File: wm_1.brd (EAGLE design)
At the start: 160 x 100 mm, 26 parts, among them IC2 DS1813-SMD, IC4 MEGA8-AI, T1 MMBT3904, T2 BT138-V, X1 MKDSN1,5/2-5,08, X2 MKDSN1,5/2-5,08

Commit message: wip
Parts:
- added R8, R9: 1k, rcl:R1206
- added SJ1: (no value), MyLib:SOLDERJUMPER_REFLOW
- moved C3 75.3 mm to (72.1, 7.68), turned to 180 degrees
- moved C16 70.3 mm to (35.3, -21.8), turned to 270 degrees
- moved C18 66.4 mm to (35.6, 3.81)
- moved C17 66.2 mm to (45.5, 3.94)
- moved Q1 66.1 mm to (40.2, -3.30)
- moved R5 65.1 mm to (78.4, 7.68)
- moved R7 63.6 mm to (72.1, 15.9), turned to 180 degrees
- moved IC4 62.2 mm to (36.0, -13.1)
- moved JP1 57.9 mm to (22.2, -15.4)
- moved R6 57.6 mm to (78.4, 15.9), turned to 180 degrees
- moved C4 56.8 mm to (72.1, 11.9), turned to 180 degrees
- moved IC2 56.3 mm to (21.0, -5.52)
- moved OK2 38.1 mm to (61.5, 11.7)
- moved C1 35.2 mm to (36.7, 49.1)
- moved C2 35.2 mm to (68.5, 49.1)
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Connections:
- new net N$17: OK2.1, R8.1
- new net N$18: OK1.5, R9.2, SJ1.1
- net +5V: now also R9.1
- net 485_R/W: now also R8.2; no longer OK2.1
- net GND: now also OK1.4
- net GROUND: now also R1.1, X1.2; no longer R2.1, X1.1
- net HOT: now also R2.1, X1.1; no longer R1.1, X1.2
- net INT0: now also SJ1.2

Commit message: wip
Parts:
- removed X1, X2: MKDSN1,5/2-5,08, con-phoenix-508:MKDSN1,5/2-5,08
- added HLK1: HLK-PM013W, hi-link:HLK-PM01
- added IN, OUT: MKDSN1,5/2-5,08, con-phoenix-508:MKDSN1,5/2-5,08
- added U$1: 2X16LCDSIDE, MyDisplays:2X16LCDSIDE
- moved OK1 56.0 mm to (73.6, 35.0), turned to 180 degrees
- moved C16 54.1 mm to (26.8, 31.6), turned to 90 degrees
- moved R4 54.0 mm to (81.5, 41.4)
- moved R8 53.8 mm to (19.7, 11.4), turned to 90 degrees
- moved R9 42.3 mm to (15.7, 11.4)
- moved SJ1 39.5 mm to (16.5, 15.8), turned to 0 degrees
- moved JP1 38.8 mm to (42.5, 17.7), flipped to the bottom, turned to 270 degrees
- moved IC4 36.1 mm to (26.5, 21.7), turned to 90 degrees
- moved IC2 27.6 mm to (43.5, 10.5), turned to 180 degrees
- moved C17 20.0 mm to (25.7, 6.41), turned to 180 degrees
- moved Q1 18.0 mm to (29.7, 11.3), turned to 180 degrees
- moved C1 15.0 mm to (51.4, 52.5)
- moved T2 14.5 mm to (97.9, 13.4), flipped to the bottom, turned to 180 degrees
- moved B1 11.5 mm to (71.9, 50.7)
- moved D1 11.5 mm to (61.5, 50.9)
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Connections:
- net 485_R/W renamed ON/OFF
- removed net N$10: IC4.23
- removed net N$11: IC4.24
- removed net N$12: IC4.25
- removed net N$13: IC4.26
- removed net SPI0: IC4.19
- new net D4: IC4.23, U$1.11
- new net D5: IC4.24, U$1.12
- new net D6: IC4.25, U$1.13
- new net D7: IC4.26, U$1.14
- new net E: IC4.22, U$1.6
- new net RS: IC4.19, U$1.4
- net +5V: now also HLK1.P$4
- net GND: now also HLK1.P$3
- net GROUND: now also HLK1.P$2, IN.2, OUT.1, R2.1; no longer R1.1, X1.2, X2.2
- net HOT: now also HLK1.P$1, IN.1, R1.1; no longer R2.1, X1.1
- net INT0: no longer SJ1.2
- net INT1: now also SJ1.2
- net LOAD: now also OUT.2; no longer X2.1
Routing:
- net HOT: track 0.00 -> 66.2 mm, vias 0 -> 1
- net LOAD: track 0.00 -> 46.2 mm
- net RESET: track 0.00 -> 45.4 mm, vias 0 -> 2
- net GROUND: track 0.00 -> 33.2 mm
- net SCK: track 0.00 -> 27.0 mm
- net N$5: track 24.6 -> 50.0 mm
- net +5V: track 0.00 -> 22.4 mm
- net GND: track 0.00 -> 21.9 mm
- net N$7: track 0.00 -> 17.6 mm
- net MISO: track 0.00 -> 17.2 mm
- net MOSI: track 0.00 -> 16.4 mm
- net N$14: track 0.00 -> 14.1 mm
- net N$26: track 0.00 -> 12.5 mm
- net N$8: track 0.00 -> 7.45 mm
- net N$16: track 0.00 -> 6.13 mm
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
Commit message: wip
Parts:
- moved R9 48.5 mm to (62.0, 26.0), turned to 180 degrees
- moved SJ1 39.8 mm to (54.9, 26.4), turned to 180 degrees
- moved R8 39.0 mm to (58.5, 15.0), turned to 180 degrees
- moved C18 30.2 mm to (9.59, -11.9)
- moved C17 30.2 mm to (1.71, -11.9)
- moved Q1 30.2 mm to (5.65, -6.99)
- moved IC4 13.5 mm to (27.0, 35.1)
- moved OK1 13.0 mm to (60.6, 35.3)
- moved C16 12.6 mm to (26.4, 44.2), turned to 180 degrees
- moved R4 11.8 mm to (69.8, 39.9), turned to 0 degrees
- moved C3 7.69 mm to (78.1, 8.45)
- moved C4 7.69 mm to (78.1, 12.6)
- moved R7 7.69 mm to (78.1, 16.6)
- moved HLK1 7.69 mm to (74.3, 12.4)
- moved OK2 7.69 mm to (67.6, 12.4)
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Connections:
- net N$14: no longer IC4.8
- net N$26: no longer IC4.7
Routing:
- net GND: track 21.9 -> 158.1 mm
- net +5V: track 22.4 -> 77.1 mm
- net RS: track 0.00 -> 27.0 mm
- net E: track 0.00 -> 19.7 mm
- net D7: track 0.00 -> 17.6 mm
- net D5: track 0.00 -> 16.6 mm
- net D4: track 0.00 -> 16.0 mm
- net RESET: track 45.4 -> 60.5 mm
- net MISO: track 17.2 -> 32.0 mm
- net MOSI: track 16.4 -> 31.2 mm
- net SCK: track 27.0 -> 41.7 mm
- net N$7: track 17.6 -> 3.46 mm
- net D6: track 0.00 -> 12.0 mm
- net N$18: track 0.00 -> 9.91 mm
- net N$5: track 50.0 -> 43.9 mm
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
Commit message: wip
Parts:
- removed C16: 0.1, rcl:C0805
- removed C17, C18: (no value), rcl:C0805
- removed IC4: MEGA8-AI, atmel:TQFP32-08
- removed Q1: (no value), crystal:SM49
- removed SJ1: (no value), MyLib:SOLDERJUMPER_REFLOW
- removed U$1: 2X16LCDSIDE, MyDisplays:2X16LCDSIDE
- added IC1: TINY13-20MM0, atmel:10M1
- moved IN 87.1 mm to (16.6, 66.7), turned to 90 degrees
- moved T2 76.2 mm to (50.0, 68.3), turned to 0 degrees
- moved R1 74.3 mm to (12.3, 46.0), turned to 0 degrees
- moved R2 74.0 mm to (12.3, 51.1), turned to 0 degrees
- moved C2 61.2 mm to (18.7, 48.6), turned to 90 degrees
- moved IC2 57.4 mm to (96.3, 32.1)
- moved R8 53.7 mm to (101.1, 47.7), turned to 0 degrees
- moved JP1 49.1 mm to (87.2, 36.9), turned to 0 degrees
- moved HLK1 48.9 mm to (27.7, 27.2), turned to 180 degrees
- moved R5 46.7 mm to (75.2, 54.2), turned to 180 degrees
- moved C3 45.9 mm to (81.5, 54.2), turned to 0 degrees
- moved B1 45.3 mm to (26.7, 48.5), turned to 90 degrees
- moved OK2 45.0 mm to (92.1, 50.2), turned to 90 degrees
- moved C4 37.6 mm to (81.5, 50.0), turned to 0 degrees
- moved OUT 34.9 mm to (107.8, 66.9)
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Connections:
- removed net D4: IC4.23, U$1.11
- removed net D5: IC4.24, U$1.12
- removed net D6: IC4.25, U$1.13
- removed net D7: IC4.26, U$1.14
- removed net E: IC4.22, U$1.6
- removed net E_RESET: IC4.13
- removed net E_SELECT: IC4.14
- removed net INT0: IC4.32
- removed net INT1: IC4.1, SJ1.2
- removed net N$14: C18.1, Q1.1
- removed net N$18: OK1.5, R9.2, SJ1.1
- removed net N$26: C17.2, Q1.2
- removed net N$61: C16.1, IC4.20
- removed net N$64: IC4.10
- removed net N$66: IC4.9
- removed net RS: IC4.19, U$1.4
- removed net RXD: IC4.30
- removed net SCL: IC4.28
- removed net SDA: IC4.27
- removed net SD_DETECT: IC4.11
- removed net SD_SELECT: IC4.12
- removed net TXD: IC4.31
- new net ZERO: OK1.5, R9.2
- net +5V: now also IC1.10; no longer IC4.18, IC4.4, IC4.6
- net GND: now also IC1.11, IC1.5; no longer C16.2, C17.1, C18.2, IC4.21, IC4.3, IC4.5
- net MISO: now also IC1.7; no longer IC4.16
- net MOSI: now also IC1.6; no longer IC4.15
- net ON/OFF: now also IC1.4; no longer IC4.2
- net RESET: now also IC1.1; no longer IC4.29
- net SCK: now also IC1.9; no longer IC4.17
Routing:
- net GND: track 158.1 -> 6.12 mm
- net +5V: track 77.1 -> 2.80 mm
- net HOT: track 71.1 -> 8.28 mm, vias 1 -> 0
- net LOAD: track 46.2 -> 6.54 mm
- net GROUND: track 38.2 -> 0.11 mm
- net SCK: track 41.7 -> 10.8 mm
- net RESET: track 60.5 -> 31.0 mm, vias 2 -> 0
- net RS: track 27.0 -> 0.00 mm
- net MISO: track 32.0 -> 6.37 mm
- net N$7: track 3.46 -> 25.1 mm
- net MOSI: track 31.2 -> 9.68 mm
- net E: track 19.7 -> 0.00 mm
- net D7: track 17.6 -> 0.00 mm
- net D5: track 16.6 -> 0.00 mm
- net D4: track 16.0 -> 0.00 mm
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
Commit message: wip
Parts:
- removed HLK1: HLK-PM013W, hi-link:HLK-PM01
- removed IC1: TINY13-20MM0, atmel:10M1
- removed IC2: DS1813-SMD, MyLib:SOT-23
- removed R9: 1k, rcl:R1206
- added F1: (no value), fuse:GSH15
- JP1: device pinhead:2X03 -> pinhead:1X03
- moved IN 54.0 mm to (4.06, 14.2), turned to 270 degrees
- moved OUT 52.9 mm to (109.1, 14.0), turned to 90 degrees
- moved OK1 36.6 mm to (62.2, 14.2)
- moved R4 36.3 mm to (59.3, 6.67)
- moved T2 35.9 mm to (54.8, 32.7)
- moved OK2 35.7 mm to (91.2, 14.5)
- moved B1 34.2 mm to (26.3, 14.3)
- moved C1 34.2 mm to (48.2, 12.8)
- moved C2 34.2 mm to (18.3, 14.4)
- moved D1 34.2 mm to (36.7, 14.1)
- moved R1 34.2 mm to (11.9, 11.8)
- moved R2 34.2 mm to (11.9, 16.9)
- moved R3 34.2 mm to (36.4, 10.2)
- moved T1 34.2 mm to (37.6, 20.5)
- moved C3 34.1 mm to (80.7, 20.1)
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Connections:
- net N$9 renamed GATE
- removed net +5V: HLK1.P$4, IC1.10, IC2.2, JP1.2, R9.1
- removed net MISO: IC1.7, JP1.1
- removed net MOSI: IC1.6, JP1.4
- removed net RESET: IC1.1, IC2.1, JP1.5
- removed net SCK: IC1.9, JP1.3
- new net N$9: F1.2, IN.1
- net GND: now also JP1.1; no longer HLK1.P$3, IC1.11, IC1.5, IC2.3, JP1.6
- net GROUND: now also R1.1; no longer HLK1.P$2, R2.1
- net HOT: now also F1.1, R2.1; no longer HLK1.P$1, IN.1, R1.1
- net ON/OFF: now also JP1.2; no longer IC1.4
- net ZERO: now also JP1.3; no longer R9.2
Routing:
- net GROUND: track 0.11 -> 130.4 mm
- net GATE: track 0.00 -> 81.9 mm, vias 0 -> 2
- net LOAD: track 6.54 -> 74.3 mm
- net ZERO: track 0.00 -> 65.4 mm
- net GND: track 6.12 -> 52.8 mm
- net RESET: track 31.0 -> 0.00 mm
- net HOT: track 8.28 -> 33.8 mm
- net SCK: track 10.8 -> 0.00 mm
- net MOSI: track 9.68 -> 0.00 mm
- net MISO: track 6.37 -> 0.00 mm
- net N$17: track 0.28 -> 6.22 mm
- net ON/OFF: track 0.00 -> 4.23 mm
- net +5V: track 2.80 -> 0.00 mm
- net N$6: track 15.4 -> 13.2 mm
- net N$16: track 6.12 -> 4.41 mm
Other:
- board size 160 x 100 mm -> 114 x 34.2 mm

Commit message: First pcb revision
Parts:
- moved T2 22.0 mm to (76.8, 31.5)
- moved F1 2.78 mm to (22.4, 27.2), flipped to the bottom, turned to 0 degrees
- moved T1 2.54 mm to (37.6, 18.0)
- moved R4 1.97 mm to (59.4, 8.64)
- moved D1 1.65 mm to (36.6, 12.4)
- moved OK1 1.52 mm to (62.2, 15.7)
- moved R3 1.48 mm to (36.2, 8.76)
- moved IN 0.19 mm to (4.06, 14.0)
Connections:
- net HOT: no longer R2.1
- net N$9: now also R2.1
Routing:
- net GATE: track 81.9 -> 149.2 mm, vias 2 -> 0
- net HOT: track 33.8 -> 63.8 mm
- net LOAD: track 74.3 -> 49.0 mm
- net N$9: track 0.00 -> 25.1 mm
- net GROUND: track 130.4 -> 122.9 mm
- net GND: track 52.8 -> 54.3 mm
- net N$4: track 15.4 -> 14.0 mm
- net N$3: track 15.2 -> 14.2 mm
- net ZERO: track 65.4 -> 64.5 mm
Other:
- board size 114 x 34.2 mm -> 114.1 x 34 mm

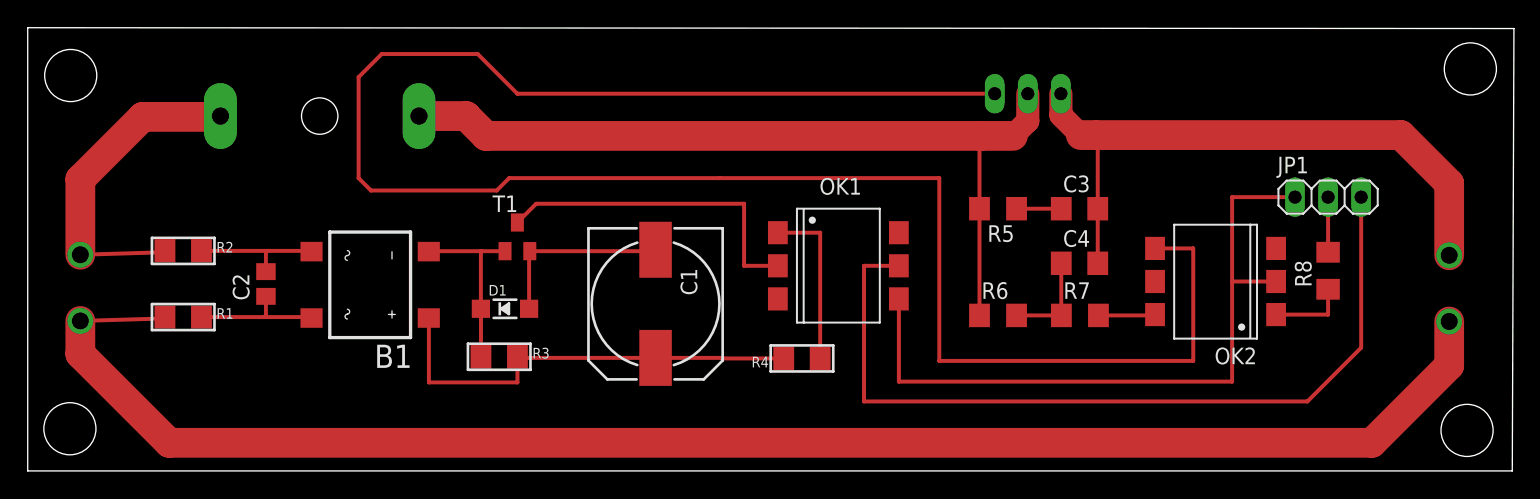
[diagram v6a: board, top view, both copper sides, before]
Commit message: Заменил разъем и сделал линии 0.5мм
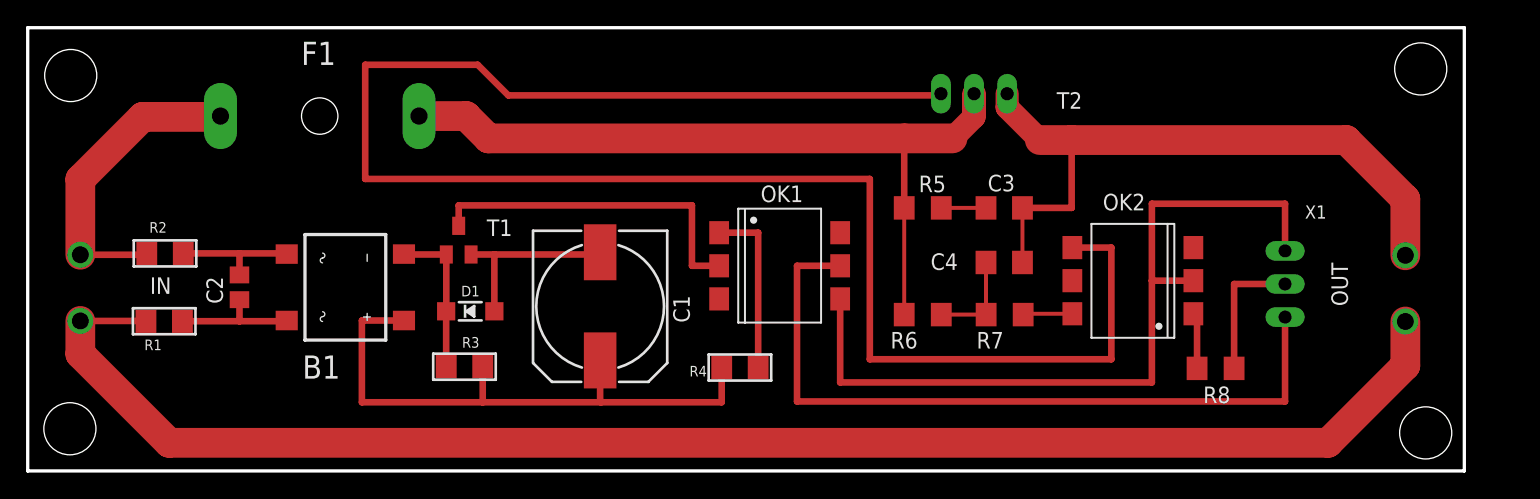
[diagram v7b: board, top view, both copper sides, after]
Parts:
- removed JP1: (no value), pinhead:1X03
- added X1: 22-23-2031, con-molex:22-23-2031
- moved R8 11.4 mm to (91.2, 7.87), turned to 0 degrees
- moved OK2 6.35 mm to (84.8, 14.6)
- moved R6 5.78 mm to (68.7, 12.0)
- moved R5 5.78 mm to (68.7, 20.2)
- moved C3 5.78 mm to (75.0, 20.2)
- moved C4 5.78 mm to (75.0, 16.0)
- moved R7 5.78 mm to (75.0, 12.0)
- moved R4 4.81 mm to (54.7, 7.94)
- moved T1 4.52 mm to (33.1, 17.7)
- moved OK1 4.51 mm to (57.7, 15.7)
- moved C1 4.26 mm to (43.9, 12.6)
- moved T2 4.13 mm to (72.6, 31.5)
- moved OUT 3.37 mm to (105.7, 14.0)
- moved R3 2.77 mm to (33.5, 8.00)
- moved D1 2.67 mm to (34.0, 12.3)
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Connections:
- net GND: now also X1.3; no longer JP1.1
- net ON/OFF: now also X1.2; no longer JP1.2
- net ZERO: now also X1.1; no longer JP1.3
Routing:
- net GATE: track 149.2 -> 136.8 mm
- net N$5: track 34.8 -> 47.1 mm
- net ZERO: track 64.5 -> 57.7 mm
- net GND: track 54.3 -> 61.1 mm
- net ON/OFF: track 4.23 -> 10.4 mm
- net GROUND: track 122.9 -> 118.2 mm
- net LOAD: track 49.0 -> 52.0 mm
- net HOT: track 63.8 -> 60.9 mm
- net N$3: track 14.2 -> 16.2 mm
- net N$4: track 14.0 -> 12.1 mm
- net N$17: track 6.22 -> 4.76 mm
- net N$9: track 25.1 -> 23.7 mm
- net N$7: track 25.4 -> 26.2 mm
- net N$16: track 4.41 -> 3.80 mm
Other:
- board size 114.1 x 34 mm -> 110.3 x 34 mm

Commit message: first revision
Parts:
- moved R2 7.16 mm to (16.3, 21.0), turned to 270 degrees
- moved R1 7.03 mm to (16.3, 7.49), turned to 90 degrees
- moved IN 3.24 mm to (7.30, 14.0)
- moved F1 0.57 mm to (21.8, 27.2)
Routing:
- net GROUND: track 118.2 -> 111.6 mm
- net N$9: track 23.7 -> 20.4 mm
- net LOAD: track 52.0 -> 49.6 mm
- net N$1: track 9.97 -> 8.19 mm
- net N$2: track 9.69 -> 8.28 mm
- net ZERO: track 57.7 -> 56.4 mm
- net GND: track 61.1 -> 59.9 mm
- net HOT: track 60.9 -> 61.5 mm
